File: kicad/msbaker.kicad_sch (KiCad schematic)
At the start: 30 parts

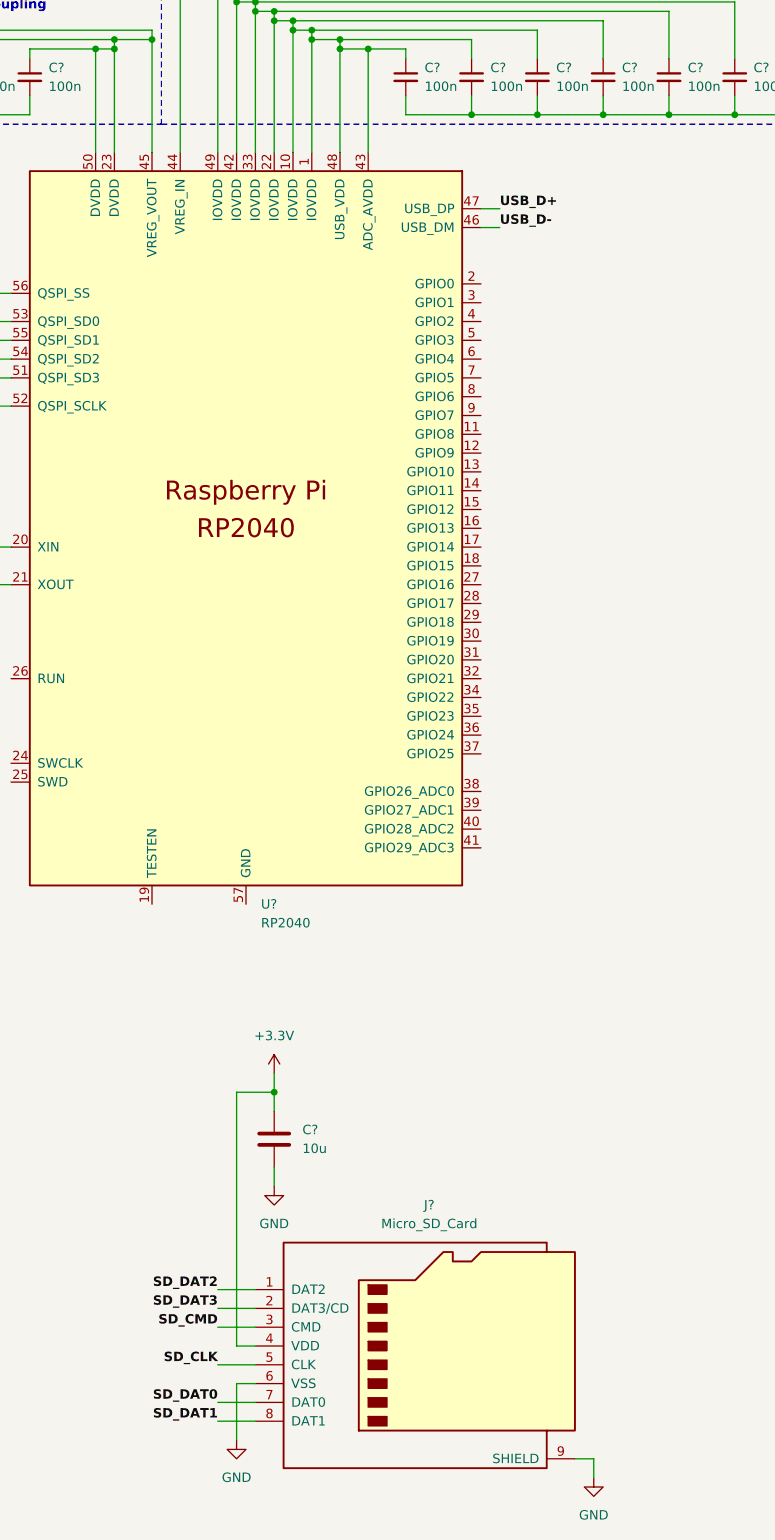
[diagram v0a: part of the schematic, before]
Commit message: Added in-series resistors for the USB data lines
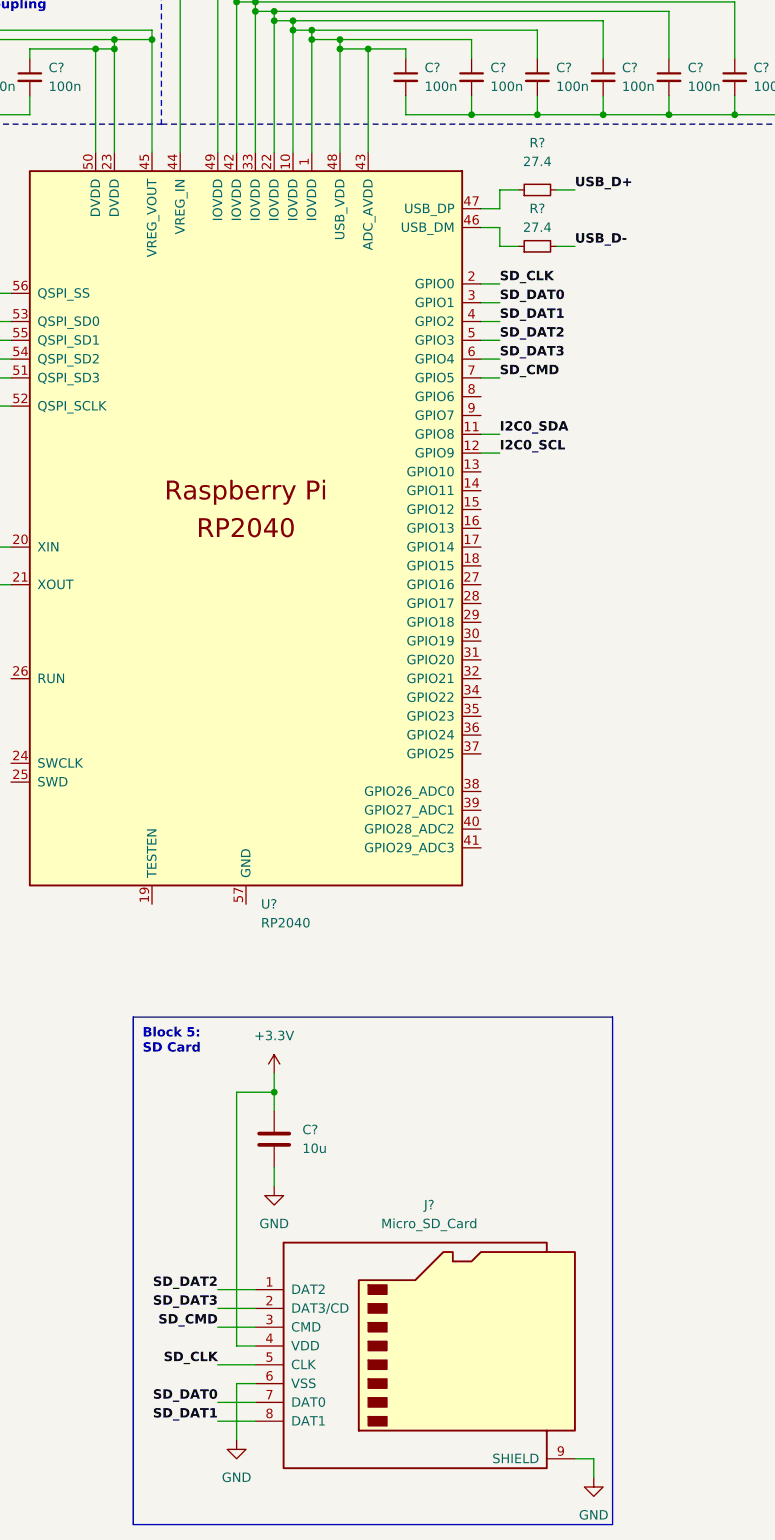
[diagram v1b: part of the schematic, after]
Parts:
- added R? (x2): 27.4, symbol Device:R_Small
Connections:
- net I2C0_SCL: now also U?.12 (GPIO9)
- net I2C0_SDA: now also U?.11 (GPIO8)
- net SD_CLK: now also U?.2 (GPIO0)
- net SD_CMD: now also U?.7 (GPIO5)
- net SD_DAT0: now also U?.3 (GPIO1)
- net SD_DAT1: now also U?.4 (GPIO2)
- net SD_DAT2: now also U?.5 (GPIO3)
- net SD_DAT3: now also U?.6 (GPIO4)
- net USB_D+: now also R?.2; no longer U?.47 (USB_DP)
- net USB_D-: now also R?.2; no longer U?.46 (USB_DM)
- new net: R?.1, U?.47 (USB_DP)
- new net: R?.1, U?.46 (USB_DM)
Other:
- note added: "Block 5: SD Card"
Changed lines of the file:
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@@
+    (stroke (width 0) (type default) (color 0 0 0 0))
+  )
+  (wire (pts (xy 365.76 213.36) (xy 368.3 213.36))
     (stroke (width 0) (type default) (color 0 0 0 0))
   )
@@
     (stroke (width 0) (type default) (color 0 0 0 0))
   )
+  (wire (pts (xy 365.76 193.04) (xy 368.3 193.04))
+    (stroke (width 0) (type default) (color 0 0 0 0))
+  )
   (polyline (pts (xy 433.07 142.24) (xy 322.58 142.24))
     (stroke (width 0) (type dot) (color 0 0 0 0))
@@
     (stroke (width 0) (type default) (color 0 0 0 0))
   )
+  (polyline (pts (xy 318.77 292.1) (xy 383.54 292.1))
+    (stroke (width 0) (type default) (color 0 0 0 0))
+  )
   (wire (pts (xy 355.6 170.18) (xy 364.49 170.18))
     (stroke (width 0) (type default) (color 0 0 0 0))
@@
     (stroke (width 0) (type default) (color 0 0 0 0))
   )
+  (wire (pts (xy 375.92 180.34) (xy 378.46 180.34))
+    (stroke (width 0) (type default) (color 0 0 0 0))
+  )
+  (wire (pts (xy 368.3 187.96) (xy 370.84 187.96))
+    (stroke (width 0) (type default) (color 0 0 0 0))
+  )
   (polyline (pts (xy 274.32 238.76) (xy 274.32 212.09))
     (stroke (width 0) (type dot) (color 0 0 0 0))
@@
     (stroke (width 0) (type default) (color 0 0 0 0))
   )
+  (wire (pts (xy 365.76 182.88) (xy 368.3 182.88))
+    (stroke (width 0) (type default) (color 0 0 0 0))
+  )
   (wire (pts (xy 279.4 184.15) (xy 279.4 198.12))
     (stroke (width 0) (type default) (color 0 0 0 0))
   )
+  (wire (pts (xy 375.92 187.96) (xy 378.46 187.96))
+    (stroke (width 0) (type default) (color 0 0 0 0))
+  )
   (wire (pts (xy 262.89 236.22) (xy 262.89 233.68))
     (stroke (width 0) (type default) (color 0 0 0 0))
@@
   )
   (wire (pts (xy 134.62 180.34) (xy 121.92 180.34))
+    (stroke (width 0) (type default) (color 0 0 0 0))
+  )
+  (wire (pts (xy 368.3 185.42) (xy 368.3 187.96))
     (stroke (width 0) (type default) (color 0 0 0 0))
   )
@@
     (stroke (width 0) (type default) (color 0 0 0 0))
   )
+  (wire (pts (xy 365.76 185.42) (xy 368.3 185.42))
+    (stroke (width 0) (type default) (color 0 0 0 0))
+  )
   (wire (pts (xy 106.68 172.72) (xy 106.68 170.18))
     (stroke (width 0) (type default) (color 0 0 0 0))
@@
     (stroke (width 0) (type default) (color 0 0 0 0))
   )
+  (polyline (pts (xy 383.54 360.68) (xy 383.54 292.1))
+    (stroke (width 0) (type default) (color 0 0 0 0))
+  )
   (wire (pts (xy 109.22 167.64) (xy 111.76 167.64))
     (stroke (width 0) (type default) (color 0 0 0 0))
@@
   )
   (wire (pts (xy 316.23 160.02) (xy 321.31 160.02))
+    (stroke (width 0) (type default) (color 0 0 0 0))
+  )
+  (wire (pts (xy 365.76 205.74) (xy 368.3 205.74))
     (stroke (width 0) (type default) (color 0 0 0 0))
   )
@@
     (stroke (width 0) (type default) (color 0 0 0 0))
   )
+  (wire (pts (xy 368.3 180.34) (xy 370.84 180.34))
+    (stroke (width 0) (type default) (color 0 0 0 0))
+  )
   (wire (pts (xy 337.82 156.21) (xy 391.16 156.21))
     (stroke (width 0) (type default) (color 0 0 0 0))
@@
     (stroke (width 0) (type default) (color 0 0 0 0))
   )
+  (wire (pts (xy 365.76 215.9) (xy 368.3 215.9))
+    (stroke (width 0) (type default) (color 0 0 0 0))
+  )
   (wire (pts (xy 260.35 166.37) (xy 260.35 168.91))
     (stroke (width 0) (type default) (color 0 0 0 0))
@@
     (stroke (width 0) (type default) (color 0 0 0 0))
   )
+  (wire (pts (xy 365.76 200.66) (xy 368.3 200.66))
+    (stroke (width 0) (type default) (color 0 0 0 0))
+  )
+  (wire (pts (xy 365.76 195.58) (xy 368.3 195.58))
+    (stroke (width 0) (type default) (color 0 0 0 0))
+  )
   (wire (pts (xy 238.76 186.69) (xy 241.3 186.69))
     (stroke (width 0) (type default) (color 0 0 0 0))
@@
     (stroke (width 0) (type default) (color 0 0 0 0))
   )
-  (wire (pts (xy 365.76 185.42) (xy 368.3 185.42))
-    (stroke (width 0) (type default) (color 0 0 0 0))
-  )
   (wire (pts (xy 299.72 226.06) (xy 299.72 228.6))
     (stroke (width 0) (type default) (color 0 0 0 0))
@@
   )
   (wire (pts (xy 468.63 245.11) (xy 471.17 245.11))
+    (stroke (width 0) (type default) (color 0 0 0 0))
+  )
+  (wire (pts (xy 365.76 198.12) (xy 368.3 198.12))
     (stroke (width 0) (type default) (color 0 0 0 0))
   )
@@
     (stroke (width 0) (type default) (color 0 0 0 0))
   )
+  (wire (pts (xy 365.76 203.2) (xy 368.3 203.2))
+    (stroke (width 0) (type default) (color 0 0 0 0))
+  )
   (wire (pts (xy 316.23 175.26) (xy 316.23 161.29))
     (stroke (width 0) (type default) (color 0 0 0 0))
@@
     (stroke (width 0) (type dot) (color 0 0 0 0))
   )
+  (polyline (pts (xy 318.77 360.68) (xy 383.54 360.68))
+    (stroke (width 0) (type default) (color 0 0 0 0))
+  )
   (wire (pts (xy 400.05 170.18) (xy 408.94 170.18))
     (stroke (width 0) (type default) (color 0 0 0 0))
@@
     (stroke (width 0) (type default) (color 0 0 0 0))
   )
-  (wire (pts (xy 365.76 182.88) (xy 368.3 182.88))
-    (stroke (width 0) (type default) (color 0 0 0 0))
-  )
   (wire (pts (xy 346.71 161.29) (xy 350.52 161.29))
     (stroke (width 0) (type default) (color 0 0 0 0))
@@
     (stroke (width 0) (type default) (color 0 0 0 0))
   )
+  (wire (pts (xy 368.3 182.88) (xy 368.3 180.34))
+    (stroke (width 0) (type default) (color 0 0 0 0))
+  )
   (wire (pts (xy 337.82 312.42) (xy 337.82 314.96))
     (stroke (width 0) (type default) (color 0 0 0 0))
@@
   )
   (wire (pts (xy 241.3 186.69) (xy 243.84 186.69))
+    (stroke (width 0) (type default) (color 0 0 0 0))
+  )
+  (polyline (pts (xy 318.77 292.1) (xy 318.77 360.68))
     (stroke (width 0) (type default) (color 0 0 0 0))
   )
@@
   )
   (text "Block 4:\nUSB" (at 118.11 248.92 0)
+    (effects (font (size 1.27 1.27) bold) (justify left bottom))
+  )
+  (text "Block 5:\nSD Card" (at 320.04 297.18 0)
     (effects (font (size 1.27 1.27) bold) (justify left bottom))
   )
@@
     (effects (font (size 1.27 1.27) bold) (justify right bottom))
   )
-  (label "USB_D+" (at 368.3 182.88 0)
+  (label "USB_D+" (at 378.46 180.34 0)
     (effects (font (size 1.27 1.27) bold) (justify left bottom))
   )
@@
     (effects (font (size 1.27 1.27) bold) (justify right bottom))
   )
+  (label "SD_DAT2" (at 368.3 200.66 0)
+    (effects (font (size 1.27 1.27) bold) (justify left bottom))
+  )
   (label "USB_D-" (at 134.62 266.7 0)
     (effects (font (size 1.27 1.27) bold) (justify left bottom))
   )
+  (label "SD_CLK" (at 368.3 193.04 0)
+    (effects (font (size 1.27 1.27) bold) (justify left bottom))
+  )
+  (label "I2C0_SCL" (at 368.3 215.9 0)
+    (effects (font (size 1.27 1.27) bold) (justify left bottom))
+  )
+  (label "SD_CMD" (at 368.3 205.74 0)
+    (effects (font (size 1.27 1.27) bold) (justify left bottom))
+  )
+  (label "SD_DAT3" (at 368.3 203.2 0)
+    (effects (font (size 1.27 1.27) bold) (justify left bottom))
+  )
   (label "SD_DAT0" (at 330.2 344.17 180)
     (effects (font (size 1.27 1.27) bold) (justify right bottom))
   )
-  (label "USB_D-" (at 368.3 185.42 0)
+  (label "USB_D-" (at 378.46 187.96 0)
+    (effects (font (size 1.27 1.27) bold) (justify left bottom))
+  )
+  (label "SD_DAT1" (at 368.3 198.12 0)
     (effects (font (size 1.27 1.27) bold) (justify left bottom))
   )
@@
     (effects (font (size 1.27 1.27) bold) (justify left bottom))
   )
+  (label "I2C0_SDA" (at 368.3 213.36 0)
+    (effects (font (size 1.27 1.27) bold) (justify left bottom))
+  )
   (label "SD_DAT3" (at 330.2 331.47 180)
     (effects (font (size 1.27 1.27) bold) (justify right bottom))
@@
   (label "SD_CLK" (at 330.2 339.09 180)
     (effects (font (size 1.27 1.27) bold) (justify right bottom))
+  )
+  (label "SD_DAT0" (at 368.3 195.58 0)
+    (effects (font (size 1.27 1.27) bold) (justify left bottom))
   )
   (symbol (lib_id "Memory_Flash:W25Q128JVS") (at 256.54 189.23 0) (unit 1)
@@
     (pin "1")
   )
+  (symbol (lib_id "Device:R_Small") (at 373.38 180.34 90) (unit 1)
+    (in_bom yes) (on_board yes) (fields_autoplaced)
+    (property "Reference" "R?" (id 0) (at 373.38 173.99 90))
+    (property "Value" "27.4" (id 1) (at 373.38 176.53 90))
+    (property "Footprint" "" (id 2) (at 373.38 180.34 0)
+      (effects (font (size 1.27 1.27)) hide)
+    )
+    (property "Datasheet" "~" (id 3) (at 373.38 180.34 0)
+      (effects (font (size 1.27 1.27)) hide)
+    )
+    (pin "1")
+    (pin "2")
+  )
   (symbol (lib_id "Device:C_Small") (at 304.8 165.1 0) (unit 1)
     (in_bom yes) (on_board yes) (fields_autoplaced)
@@
     )
     (property "Datasheet" "~" (id 3) (at 304.8 165.1 0)
+      (effects (font (size 1.27 1.27)) hide)
+    )
+    (pin "1")
+    (pin "2")
+  )
+  (symbol (lib_id "Device:R_Small") (at 373.38 187.96 90) (unit 1)
+    (in_bom yes) (on_board yes)
+    (property "Reference" "R?" (id 0) (at 373.38 182.88 90))
+    (property "Value" "27.4" (id 1) (at 373.38 185.42 90))
+    (property "Footprint" "" (id 2) (at 373.38 187.96 0)
+      (effects (font (size 1.27 1.27)) hide)
+    )
+    (property "Datasheet" "~" (id 3) (at 373.38 187.96 0)
       (effects (font (size 1.27 1.27)) hide)
     )
@@
       (reference "JP?") (unit 1) (value "BOOTSEL") (footprint "")
     )
+    (path "/24808f62-cb68-4239-b41c-958ef9f78a48"
+      (reference "R?") (unit 1) (value "27.4") (footprint "")
+    )
+    (path "/28f1ba77-30d5-47ab-8a26-c9188be38f2c"
+      (reference "R?") (unit 1) (value "27.4") (footprint "")
+    )
     (path "/c4d85a1a-f456-46d9-bbdb-2829a6af88a9"
